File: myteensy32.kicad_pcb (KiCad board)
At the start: 2 copper layers, 35.6 x 17.8 mm, 31 parts, among them J1 Conn_01x14_Male, J2 Conn_01x14_Male, J3 USB_C_Receptacle_USB2.0, SW1 RESET, SW2 PROG, U1 MKL04Z32VLC4, U2 MK20DX256VLH7, U3 MCP2562-E-SN, U4 NJM2884U1, Y2 16MHz

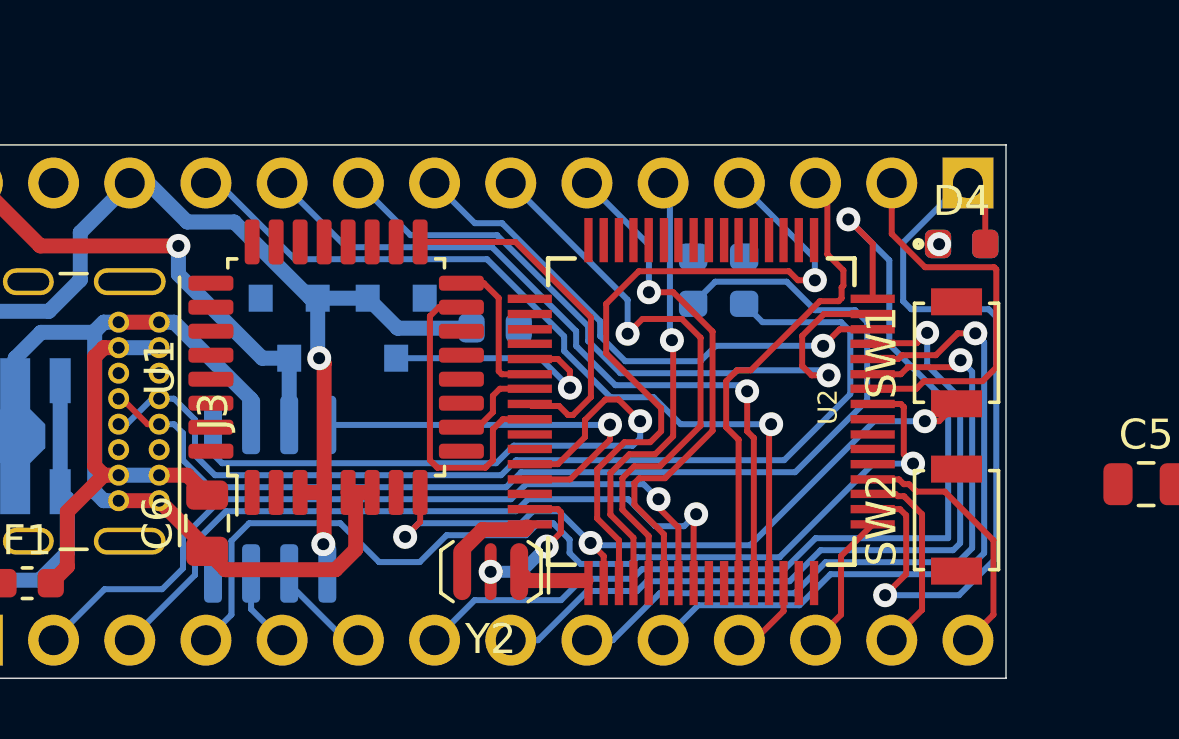
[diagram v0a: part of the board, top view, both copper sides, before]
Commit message: 許容クリアランスをfusionPCBの規約に沿ってギリギリに変更
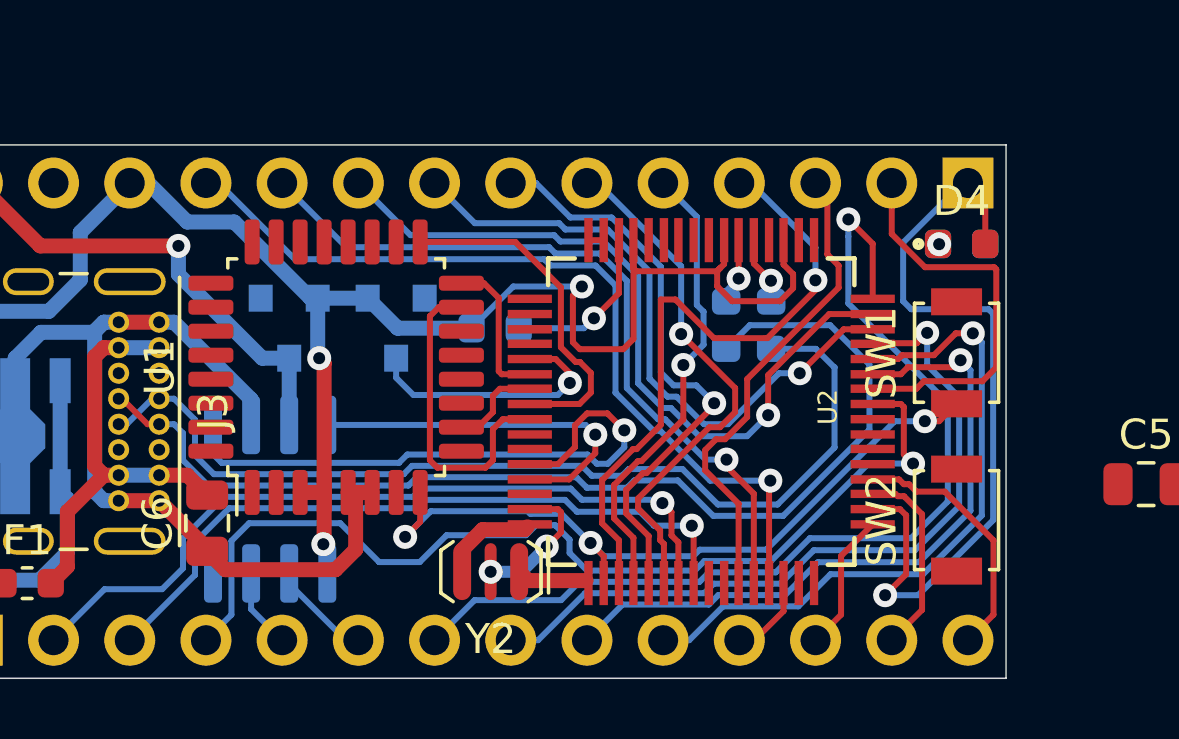
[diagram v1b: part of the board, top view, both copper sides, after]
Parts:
- moved R3 1.86 mm to (141.8, 78.4)
- moved R2 1.75 mm to (143.3, 78.4)
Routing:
- net +3V3: track 36.3 -> 58.3 mm, vias 2 -> 3
- net Net-(C7-Pad2): track 0.00 -> 5.59 mm, vias 0 -> 1
- net Net-(J1-Pad8): track 17.8 -> 21.3 mm
- net Net-(R2-Pad2): track 0.00 -> 2.29 mm, vias 0 -> 1
- net Net-(R3-Pad2): track 0.00 -> 2.22 mm, vias 0 -> 1
- net Net-(J1-Pad9): track 23.4 -> 25.2 mm
- net Net-(J1-Pad4): track 23.6 -> 21.8 mm
- net /CAN_TX: track 21.5 -> 20.3 mm
- net /USB+: track 33.6 -> 32.6 mm
- net /CAN_RX: track 13.1 -> 12.2 mm
- net Net-(J2-Pad10): track 23.1 -> 22.2 mm
- net /INTERNAL_LED: track 26.9 -> 26.1 mm
- net Net-(J2-Pad9): track 23.7 -> 22.8 mm
- net Net-(J2-Pad8): track 25.8 -> 25.0 mm
- net Net-(J2-Pad7): track 33.5 -> 32.8 mm
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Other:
- net class 0.2: clearance 0.2 -> 0.1778
- net class 0.5: clearance 0.2 -> 0.1778
- net class 1.0: clearance 0.2 -> 0.1778; via_drill 3.2 -> 3.200001
- net class Default: clearance 0.2 -> 0.1778
- rule trace_clearance: 0.2 -> 0.1778

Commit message: いったん保存
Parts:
- C1, C2, R4: moved to B.Cu
- moved C1 53.4 mm to (130.1, 86.3), turned to 270 degrees
- moved R4 44.1 mm to (118.9, 75.5)
- moved C2 42.4 mm to (125.2, 79.7)
- moved D3 38.6 mm to (117.6, 75.5)
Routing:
- net /ProgramModeBtn: track 0.00 -> 33.5 mm, vias 0 -> 2
- net GND: track 36.9 -> 64.4 mm
- net +3V3: track 58.3 -> 81.1 mm
- net /RESET: track 24.7 -> 33.6 mm
- net Net-(J1-Pad4): track 21.8 -> 15.5 mm
- net Net-(J2-Pad4): track 33.1 -> 38.7 mm
- net /CAN_RX: track 12.2 -> 16.2 mm
- net Net-(J2-Pad3): track 23.6 -> 27.0 mm
- net Net-(D3-Pad1): track 0.00 -> 3.03 mm, vias 0 -> 1
- net /INTERNAL_LED: track 26.1 -> 28.8 mm
- net Net-(J2-Pad8): track 25.0 -> 27.5 mm
- net /PTA3: track 10.7 -> 13.1 mm
- net Net-(J2-Pad2): track 26.1 -> 28.4 mm
- net +5V: track 26.3 -> 28.6 mm
- net Net-(J2-Pad10): track 22.2 -> 23.9 mm
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
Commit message: 殆どの配線が終わった。
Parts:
- C3, C4, C9: moved to B.Cu
- moved C4 70.2 mm to (145.4, 85.1)
- moved C11 58.6 mm to (128.5, 85.6), turned to 180 degrees
- moved C7 51.6 mm to (133.3, 75.5), turned to 180 degrees
- moved C8 50.0 mm to (135.3, 75.9), turned to 270 degrees
- moved C3 45.9 mm to (137.3, 75.4)
- moved C9 45.0 mm to (129.6, 81.3), turned to 270 degrees
- moved C5 27.8 mm to (134.6, 65.8), turned to 180 degrees
- moved C1 0.32 mm to (130.1, 86.0)
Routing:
- net GND: track 64.4 -> 91.0 mm, vias 2 -> 6
- net Net-(J2-Pad4): track 38.7 -> 29.9 mm
- net Net-(C7-Pad2): track 5.10 -> 12.5 mm
- net /INTERNAL_LED: track 28.8 -> 23.1 mm
- net Net-(J2-Pad7): track 34.1 -> 29.4 mm
- net +3V3: track 81.1 -> 85.7 mm, vias 3 -> 5
- net /PTA3: track 13.1 -> 10.3 mm, vias 0 -> 2
- net /PTA2: track 11.6 -> 13.9 mm
- net /RESET: track 33.6 -> 35.8 mm
- net Net-(C9-Pad1): track 7.07 -> 9.11 mm
- net /ProgramModeBtn: track 33.5 -> 35.4 mm
- net Net-(J1-Pad9): track 25.2 -> 23.3 mm
- net /CAN_TX: track 18.8 -> 17.3 mm
- net Net-(J1-Pad7): track 18.7 -> 20.2 mm
- net /CAN_RX: track 16.2 -> 14.9 mm
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- added copper zone on B.Cu, net GND
- added copper zone on F.Cu, net GND

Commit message: いったんコミット
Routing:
- net GND: track 91.0 -> 109.8 mm, vias 6 -> 9
- net Net-(J2-Pad9): track 25.2 -> 31.1 mm
- net Net-(J1-Pad10): track 27.5 -> 25.8 mm
- net +3V3: track 85.7 -> 87.3 mm
- net /USB+: track 32.2 -> 33.3 mm
- net Net-(J1-Pad8): track 20.9 -> 20.0 mm
- net Net-(J1-Pad11): track 27.5 -> 26.9 mm
- net Net-(J1-Pad9): track 23.3 -> 23.9 mm
- net /PTA2: track 13.9 -> 13.4 mm
